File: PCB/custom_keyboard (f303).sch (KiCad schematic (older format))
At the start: 320 parts, among them J1 Conn_01x04, J2 SM04B-SRSS-TB(LF)(SN), Q1 2N7002, SW1 SW_Push, U1 SRV05-4, U12 XC6206P332MR, U13 74LVC1G34, U14 STM32F303CBT6, X1 TestPoint_Small, X2 TestPoint_Small, Y2 8MHz

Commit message: Separated LED footprints into groups
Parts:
- removed LED1, LED10, LED11, LED12, LED13, LED14, LED15, LED16, LED17, LED18, LED19, LED2, LED20, LED21, LED22, LED23, LED24, LED25, LED26, LED27, LED28, LED29, LED3, LED30, LED31, LED32, LED4, LED5, LED6, LED7, LED8, LED9: RGB-6028, random-keyboard-parts:RGB-6028, symbol random-keyboard-parts:RGB-6028
- added LED1, LED10, LED11, LED12, LED13, LED14, LED15, LED16, LED17, LED18, LED19, LED2, LED20, LED21, LED22, LED23, LED24, LED25, LED26, LED27, LED28, LED29, LED3, LED30, LED31, LED32, LED33, LED34, LED35, LED36, LED37, LED38, LED39, LED4, LED40, LED41, LED42, LED43, LED44, LED45, LED46, LED47, LED48, LED49, LED5, LED50, LED51, LED52, LED53, LED54, LED55, LED56, LED57, LED58, LED59, LED6, LED60, LED61, LED62, LED63, LED64, LED65, LED66, LED67, LED68, LED69, LED7, LED70, LED71, LED72, LED73, LED74, LED75, LED76, LED77, LED78, LED79, LED8, LED80, LED81, LED82, LED83, LED84, LED85, LED86, LED87, LED88, LED89, LED9, LED90: LED_ARGB, random-keyboard-parts:RGB-6028, symbol Device:LED_ARGB
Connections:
- wire segments 1326 -> 1967
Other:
- moved on the sheet: C10, C11, C12, C13, C5, C6, I1, I2, I3, R10, R11, R14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

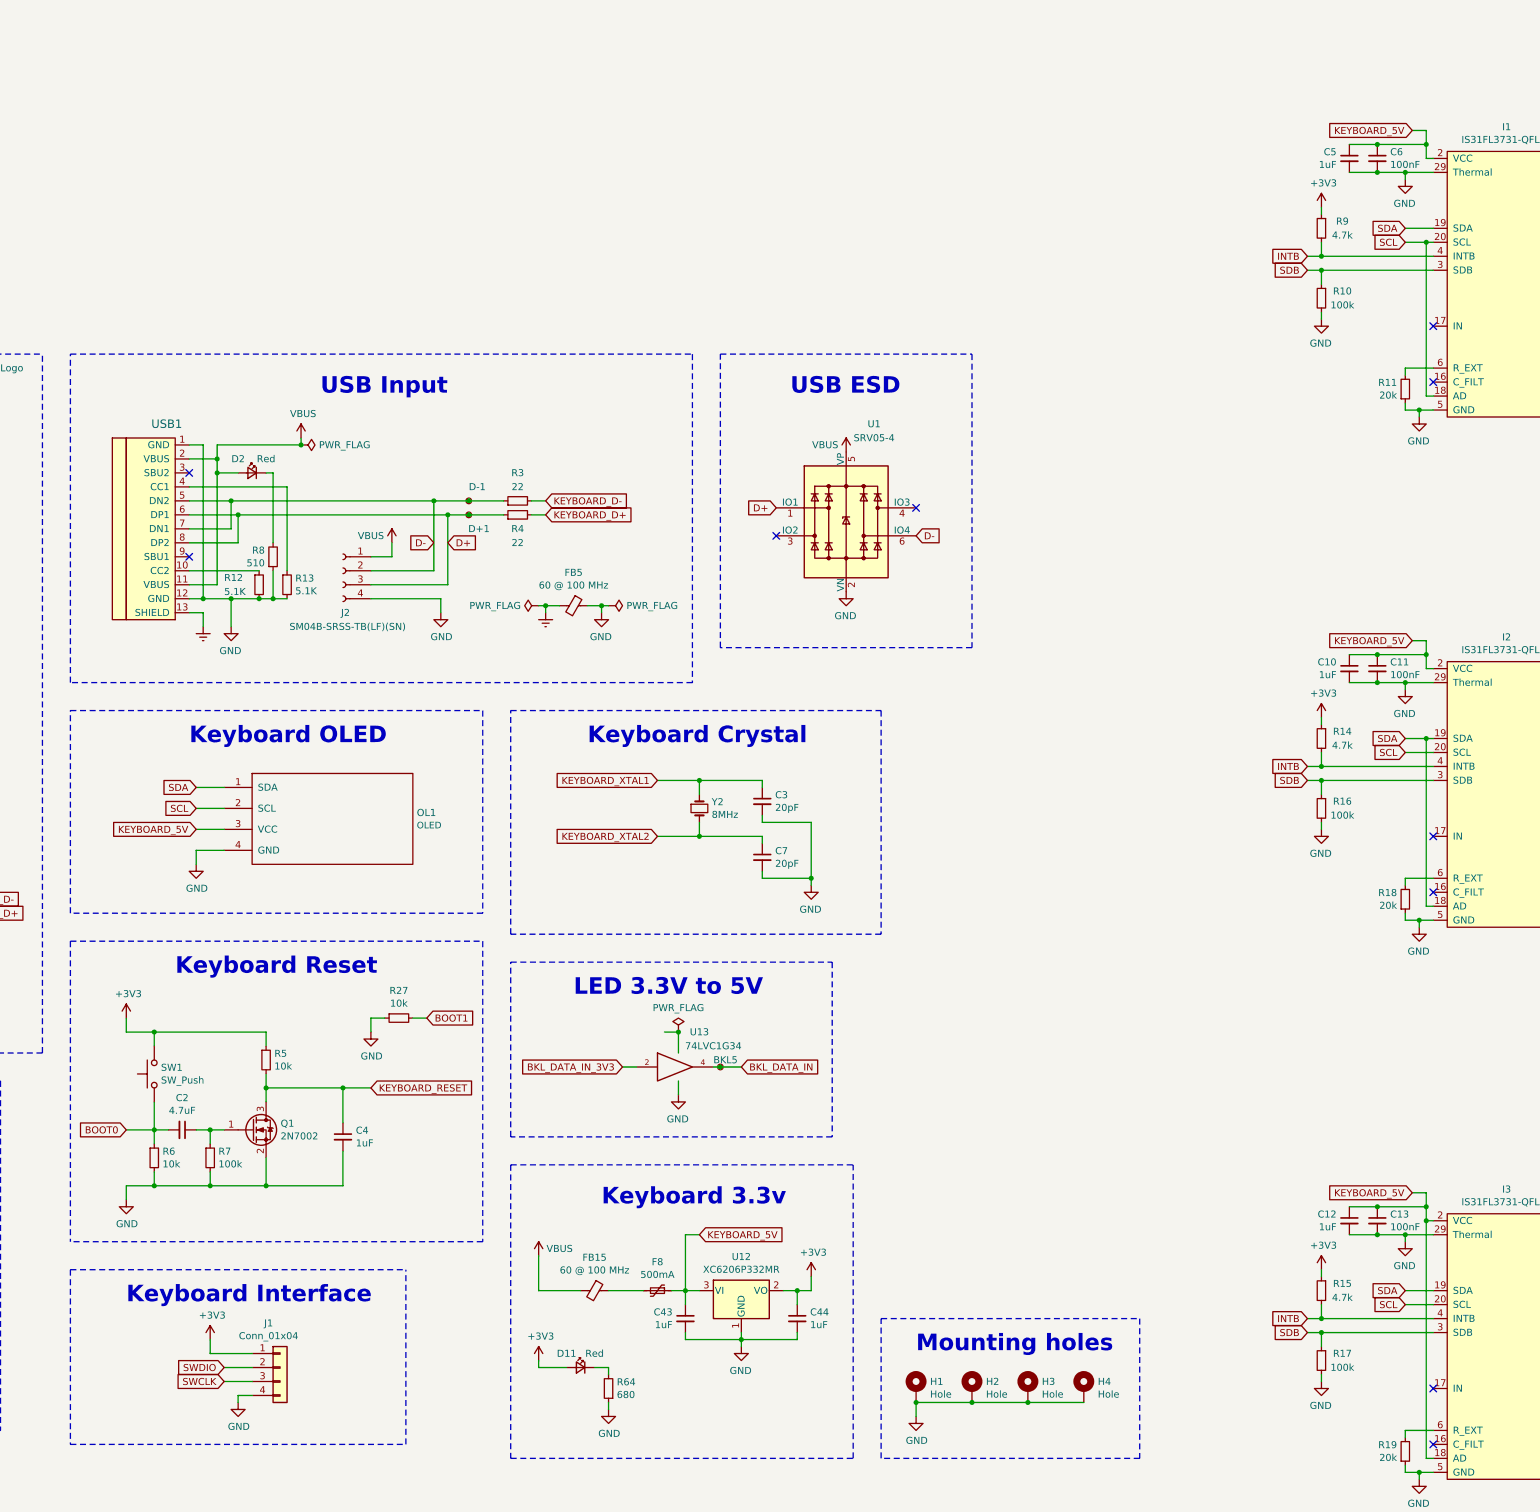
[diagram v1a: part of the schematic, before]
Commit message: Replaced KEYBOARD_5V with VCC
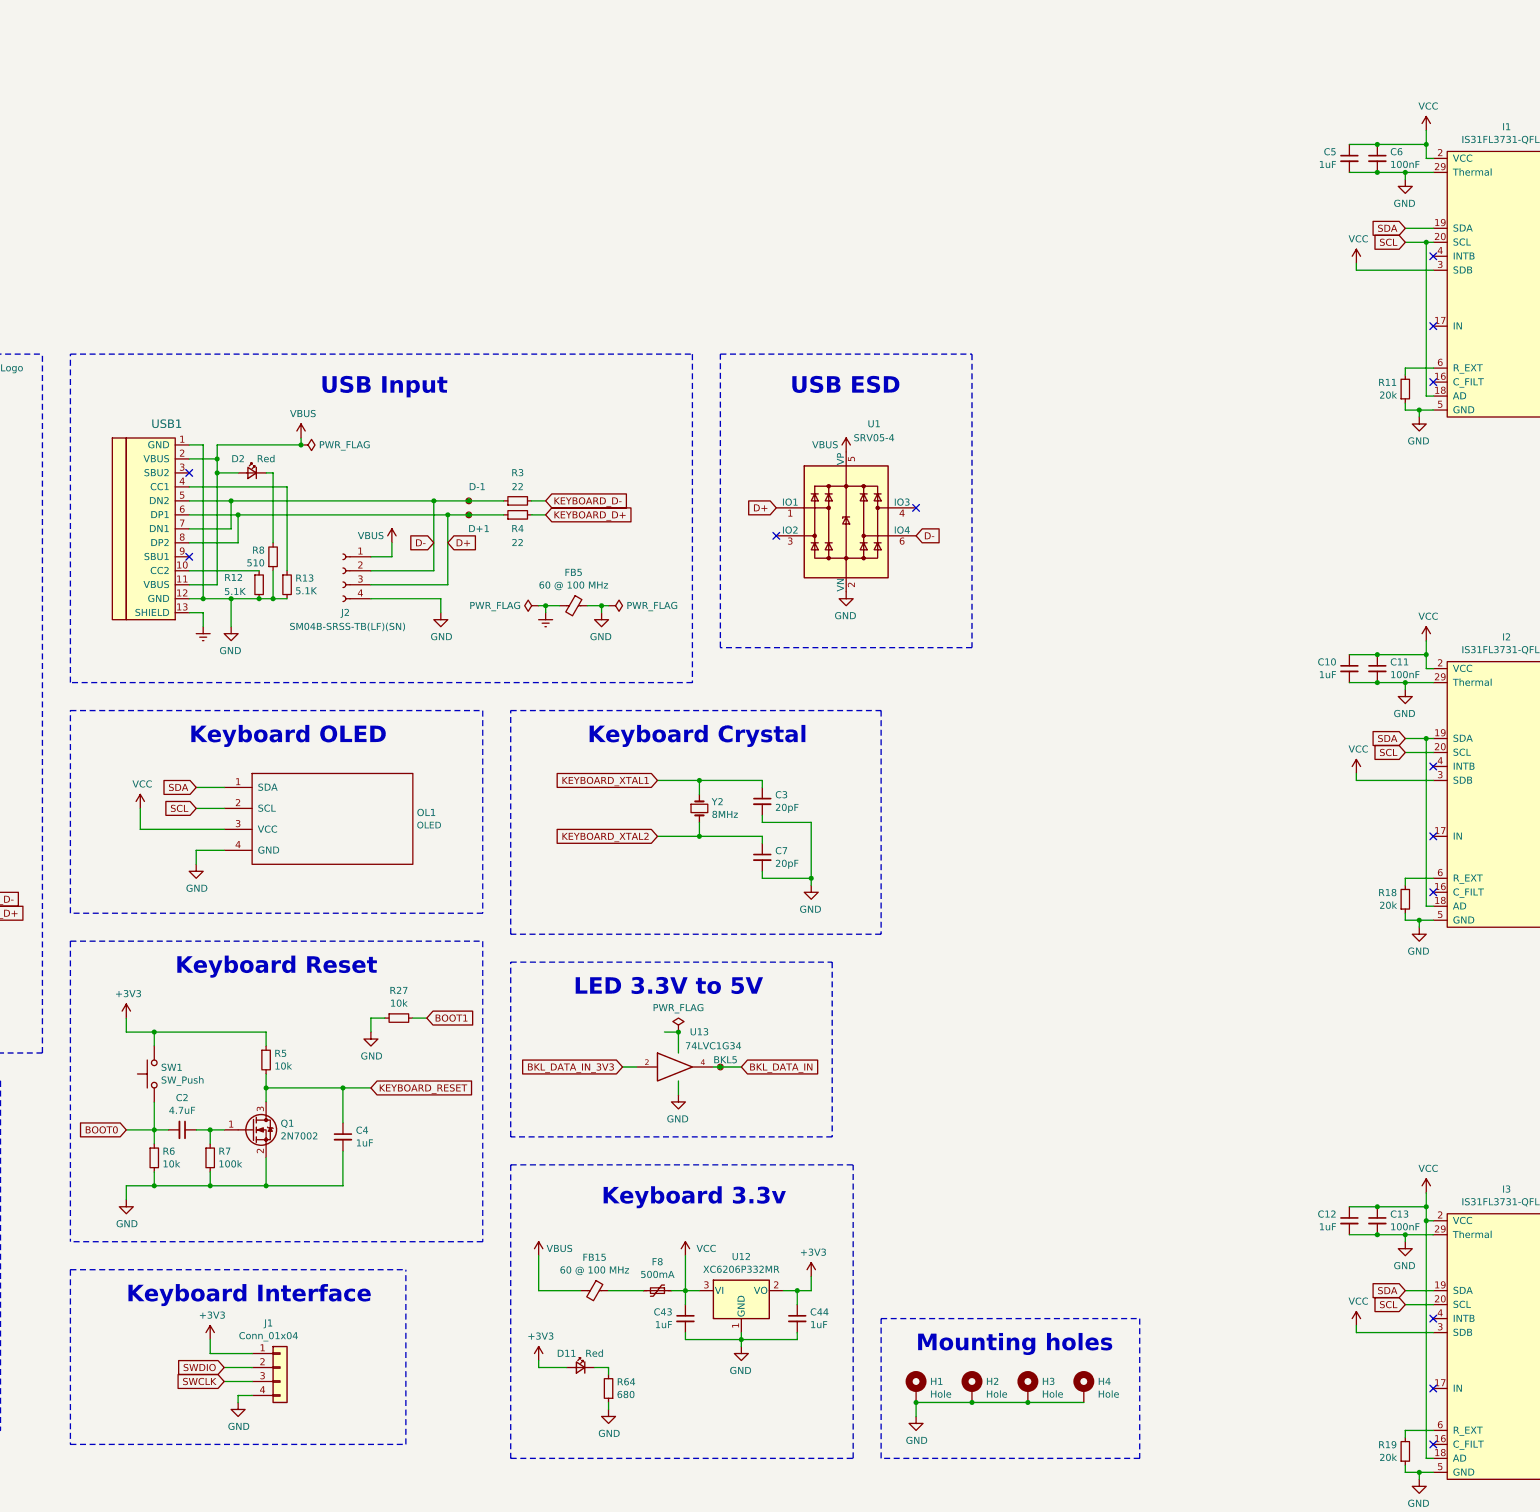
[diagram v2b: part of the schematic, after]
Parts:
- removed R10, R16, R17: 100k, Resistor_SMD:R_0805_2012Metric, symbol Device:R_Small
- removed R14, R15, R9: 4.7k, Resistor_SMD:R_0805_2012Metric, symbol Device:R_Small
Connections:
- net KEYBOARD_5V is gone; now on net VCC: C10.1, C11.1, C12.1, C13.1, C43.1, C5.1, C6.1, F8.1, I1.2 (VCC), I2.2 (VCC), I3.18 (AD), I3.2 (VCC), OL1.3 (VCC), U12.3 (VI)
- net SDB is gone; now on net VCC: I1.3 (SDB), I2.3 (SDB), I3.3 (SDB)
- removed net INTB: I1.4 (INTB), I2.4 (INTB), I3.4 (INTB)
- no-connect marks 11 -> 14

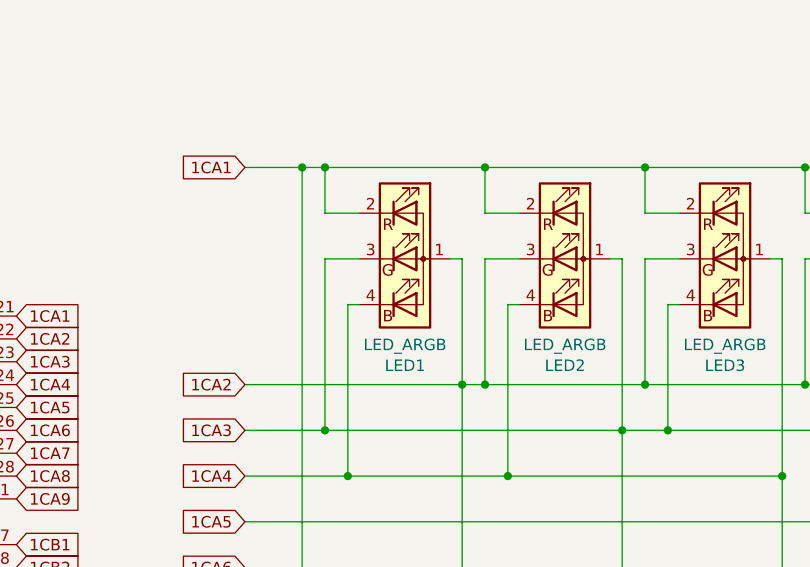
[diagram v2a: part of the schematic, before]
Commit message: Footprint for MHT151RGBCT
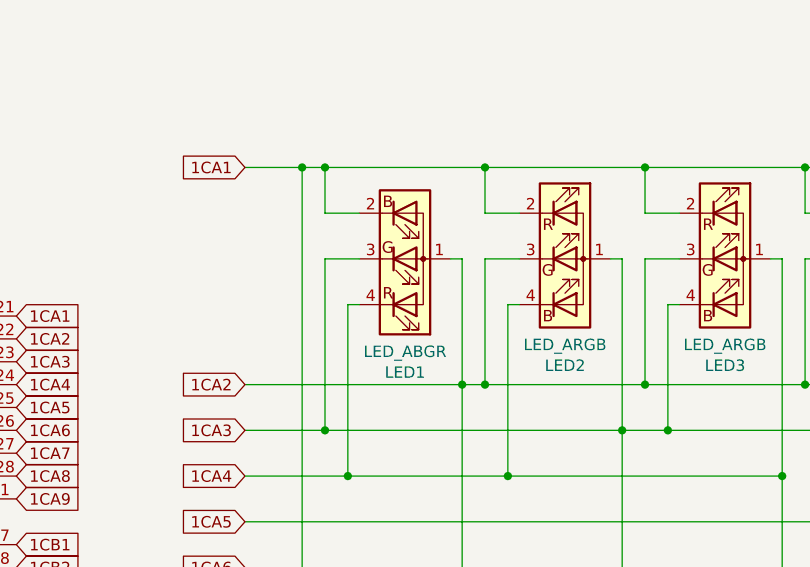
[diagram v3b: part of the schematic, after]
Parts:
- removed LED1: LED_ARGB, random-keyboard-parts:RGB-6028, symbol Device:LED_ARGB
- added LED1: LED_ABGR, custom-footprints:MHT151RGBCT_with_outline, symbol Device:LED_ABGR
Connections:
- net 1CA1: now also LED1.2 (BK)
- net 1CA2: now also LED1.1 (A)
- net 1CA3: now also LED1.3 (GK)
- net 1CA4: now also LED1.4 (RK)
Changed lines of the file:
@@
 Wire Wire Line
 	20900 10050 20750 10050
-$Comp
-L Device:LED_ARGB LED1
-U 1 1 755652E9
-P 20400 10250
-F 0 "LED1" H 20400 9783 50  0000 C CNN
-F 1 "LED_ARGB" H 20400 9874 50  0000 C CNN
-F 2 "random-keyboard-parts:RGB-6028" H 20400 10200 50  0001 C CNN
-F 3 "~" H 20400 10200 50  0001 C CNN
-	1    20400 10250
-	1    0    0    -1
-$EndComp
 Wire Wire Line
 	21450 10050 21450 9850
@@
 	1    0    0    -1
 $EndComp
+$Comp
+L Device:LED_ABGR LED1
+U 1 1 61F18A29
+P 20400 10250
+F 0 "LED1" H 20400 10747 50  0000 C CNN
+F 1 "LED_ABGR" H 20400 10656 50  0000 C CNN
+F 2 "custom-footprints:MHT151RGBCT_with_outline" H 20400 10200 50  0001 C CNN
+F 3 "~" H 20400 10200 50  0001 C CNN
+	1    20400 10250
+	1    0    0    1
+$EndComp
 $EndSCHEMATC

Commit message: Removed mounting holes
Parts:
- removed H1, H2, H3, H4: Hole, MountingHole:MountingHole_3.2mm_M3_Pad, symbol Mechanical:MountingHole_Pad
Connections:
- net COL17: now also MX32.1, MX50.1
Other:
- note removed: "Mounting holes"
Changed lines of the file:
@@
 Wire Notes Line
 	7900 14450 10850 14450
-$Comp
-L power:PWR_FLAG #FLG0103
-U 1 1 9DFF72AC
-P 12250 16750
-F 0 "#FLG0103" H 12250 16825 50  0001 C CNN
-F 1 "PWR_FLAG" H 12250 16923 50  0000 C CNN
-F 2 "" H 12250 16750 50  0001 C CNN
-F 3 "~" H 12250 16750 50  0001 C CNN
-	1    12250 16750
-	1    0    0    -1
-$EndComp
 Wire Wire Line
 	11850 17000 11950 17000
@@
 Wire Wire Line
 	12250 16750 12250 16900
-Connection ~ 12250 16750
-Wire Wire Line
-	12250 16750 12150 16750
 NoConn ~ 7350 12000
 $Comp
@@
 Wire Wire Line
 	5800 15700 6050 15700
-$Comp
-L Mechanical:MountingHole_Pad H1
-U 1 1 6C24E77E
-P 13950 19300
-F 0 "H1" H 14050 19349 50  0000 L CNN
-F 1 "Hole" H 14050 19258 50  0000 L CNN
-F 2 "MountingHole:MountingHole_3.2mm_M3_Pad" H 13950 19300 50  0001 C CNN
-F 3 "~" H 13950 19300 50  0001 C CNN
-	1    13950 19300
-	1    0    0    -1
-$EndComp
-$Comp
-L power:GND #PWR0199
-U 1 1 6C24F04A
-P 13950 19500
-F 0 "#PWR0199" H 13950 19250 50  0001 C CNN
-F 1 "GND" H 13955 19327 50  0000 C CNN
-F 2 "" H 13950 19500 50  0001 C CNN
-F 3 "" H 13950 19500 50  0001 C CNN
-	1    13950 19500
-	1    0    0    -1
-$EndComp
-$Comp
-L Mechanical:MountingHole_Pad H2
-U 1 1 6C24F523
-P 14350 19300
-F 0 "H2" H 14450 19349 50  0000 L CNN
-F 1 "Hole" H 14450 19258 50  0000 L CNN
-F 2 "MountingHole:MountingHole_3.2mm_M3_Pad" H 14350 19300 50  0001 C CNN
-F 3 "~" H 14350 19300 50  0001 C CNN
-	1    14350 19300
-	1    0    0    -1
-$EndComp
-$Comp
-L Mechanical:MountingHole_Pad H3
-U 1 1 6C24F72A
-P 14750 19300
-F 0 "H3" H 14850 19349 50  0000 L CNN
-F 1 "Hole" H 14850 19258 50  0000 L CNN
-F 2 "MountingHole:MountingHole_3.2mm_M3_Pad" H 14750 19300 50  0001 C CNN
-F 3 "~" H 14750 19300 50  0001 C CNN
-	1    14750 19300
-	1    0    0    -1
-$EndComp
-$Comp
-L Mechanical:MountingHole_Pad H4
-U 1 1 6C24FA2A
-P 15150 19300
-F 0 "H4" H 15250 19349 50  0000 L CNN
-F 1 "Hole" H 15250 19258 50  0000 L CNN
-F 2 "MountingHole:MountingHole_3.2mm_M3_Pad" H 15150 19300 50  0001 C CNN
-F 3 "~" H 15150 19300 50  0001 C CNN
-	1    15150 19300
-	1    0    0    -1
-$EndComp
-Wire Wire Line
-	15150 19400 14750 19400
-Connection ~ 14350 19400
-Wire Wire Line
-	14350 19400 13950 19400
-Connection ~ 14750 19400
-Wire Wire Line
-	14750 19400 14350 19400
-Wire Wire Line
-	13950 19500 13950 19400
-Connection ~ 13950 19400
 Text GLabel 6450 15500 2    50   Input ~ 0
 A9
@@
 Text GLabel 3950 15500 0    50   Input ~ 0
 ROW5
-Text Notes 13950 19050 0    118  ~ 24
-Mounting holes
-Wire Notes Line
-	13700 18800 15550 18800
-Wire Notes Line
-	15550 18800 15550 19800
-Wire Notes Line
-	15550 19800 13700 19800
-Wire Notes Line
-	13700 19800 13700 18800
 $Comp
 L Transistor_FET:2N7002 Q1
@@
 Connection ~ 17950 3400
 Wire Wire Line
-	17950 3400 17950 8400
+	17950 3400 17950 4400
 Wire Wire Line
 	1800 3400 1900 3400
@@
 L power:VCC #PWR0101
 U 1 1 64050371
-P 12300 18350
-F 0 "#PWR0101" H 12300 18200 50  0001 C CNN
-F 1 "VCC" H 12450 18400 50  0000 C CNN
-F 2 "" H 12300 18350 50  0001 C CNN
-F 3 "" H 12300 18350 50  0001 C CNN
-	1    12300 18350
+P 12300 18200
+F 0 "#PWR0101" H 12300 18050 50  0001 C CNN
+F 1 "VCC" H 12450 18250 50  0000 C CNN
+F 2 "" H 12300 18200 50  0001 C CNN
+F 3 "" H 12300 18200 50  0001 C CNN
+	1    12300 18200
 	1    0    0    -1
 $EndComp
-Wire Wire Line
-	12300 18350 12300 18600
 $Comp
 L power:VCC #PWR0102
@@
 	1    0    0    1
 $EndComp
+$Comp
+L power:PWR_FLAG #FLG0104
+U 1 1 646AA100
+P 12300 18250
+F 0 "#FLG0104" H 12300 18325 50  0001 C CNN
+F 1 "PWR_FLAG" V 12300 18377 50  0000 L CNN
+F 2 "" H 12300 18250 50  0001 C CNN
+F 3 "~" H 12300 18250 50  0001 C CNN
+	1    12300 18250
+	0    -1   -1   0
+$EndComp
+Wire Wire Line
+	12300 18200 12300 18250
+Connection ~ 12300 18250
+Wire Wire Line
+	12300 18250 12300 18600
+Wire Wire Line
+	18150 5400 17950 5400
+Connection ~ 17950 5400
+Wire Wire Line
+	17950 5400 17950 8400
+Wire Wire Line
+	18150 4400 17950 4400
+Connection ~ 17950 4400
+Wire Wire Line
+	17950 4400 17950 5400
+$Comp
+L power:VCC #PWR0109
+U 1 1 6514B5A6
+P 12250 16750
+F 0 "#PWR0109" H 12250 16600 50  0001 C CNN
+F 1 "VCC" H 12400 16800 50  0000 C CNN
+F 2 "" H 12250 16750 50  0001 C CNN
+F 3 "" H 12250 16750 50  0001 C CNN
+	1    12250 16750
+	-1   0    0    -1
+$EndComp
 $EndSCHEMATC
